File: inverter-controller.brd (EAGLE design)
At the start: 96 x 87 mm, 164 parts, among them IC1 STM32F334C8T6, IC10 ISO3082, IC2 SY7152ABC, IC3 LMV358MMX, IC4 LMV358MMX, IC5 SY7152ABC, J1 621006245821, J2 61300211121, J3 CONNECTOR-SMD-2PIN, J4 CONNECTOR-SMD-2PIN, J5 CONNECTOR-SMD-2PIN, X3 0289-9068**15EDGVC-3.81-03P-14, X6 1365-16, Y1 NX2016SA-32M

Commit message: Opamp devreleri düzenlendi.
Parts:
- moved DC7 804.7 mm to (37.5, 50.6)
- moved C66 789.4 mm to (40.3, 60.0)
- moved R65 780.3 mm to (40.3, 62.2), turned to 180 degrees
- moved TP8 780.1 mm to (36.1, 35.4), turned to 270 degrees
- moved C61 775.3 mm to (39.0, 35.4)
- moved TP11 773.5 mm to (35.0, 45.5)
- moved C60 767.9 mm to (39.0, 33.3), turned to 180 degrees
- moved C50 760.8 mm to (32.4, 33.1), turned to 180 degrees
- moved TP7 758.8 mm to (36.0, 33.3), turned to 270 degrees
- moved R69 757.8 mm to (29.8, 36.1), turned to 90 degrees
- moved R48 755.7 mm to (43.7, 41.5), turned to 90 degrees
- moved C53 754.8 mm to (45.0, 52.9), turned to 90 degrees
- moved L1 754.1 mm to (34.2, 48.3)
- moved R66 749.6 mm to (30.8, 38.9)
- moved R41 747.0 mm to (34.1, 42.3)
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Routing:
- net IA: track 0.00 -> 29.0 mm
- net N$20: track 0.00 -> 20.9 mm
- net I_IN: track 3.49 -> 23.0 mm
- net VB: track 0.00 -> 18.9 mm
- net VA: track 0.00 -> 15.5 mm
- net VOUT: track 0.00 -> 13.7 mm
- net IB: track 3.90 -> 12.4 mm
- net VIN_2: track 0.00 -> 8.41 mm
- net VIN_1: track 3.57 -> 11.4 mm
- net GND: track 0.00 -> 7.61 mm
- net N$15: track 0.00 -> 5.77 mm
- net N$21: track 0.00 -> 5.54 mm
- net N$19: track 0.00 -> 5.40 mm
- net IB_SENS: track 0.00 -> 5.05 mm, vias 0 -> 1
- net VB_SENS: track 0.00 -> 5.03 mm, vias 0 -> 1
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
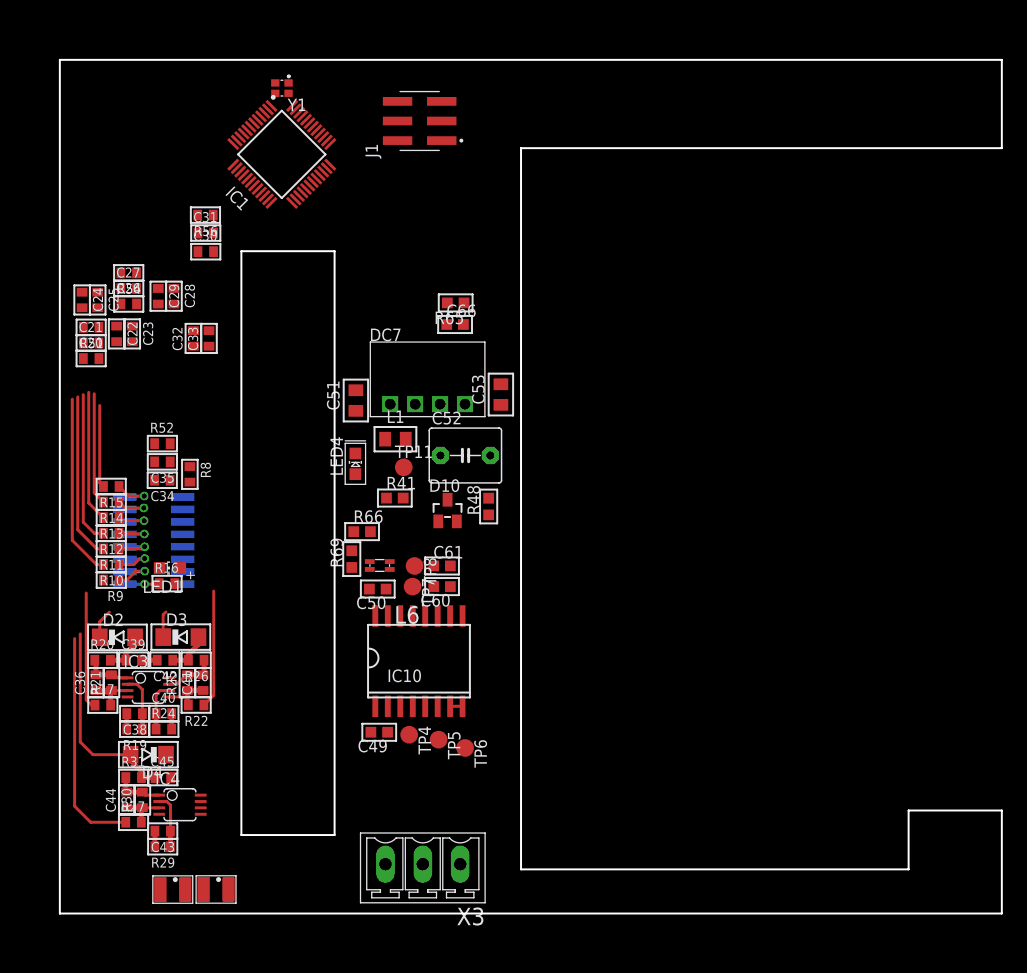
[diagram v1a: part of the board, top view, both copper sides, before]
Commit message: Dxf dosyasi cizimin uzerine eklendi, kart boyutlarinda duzenleme yapildi.
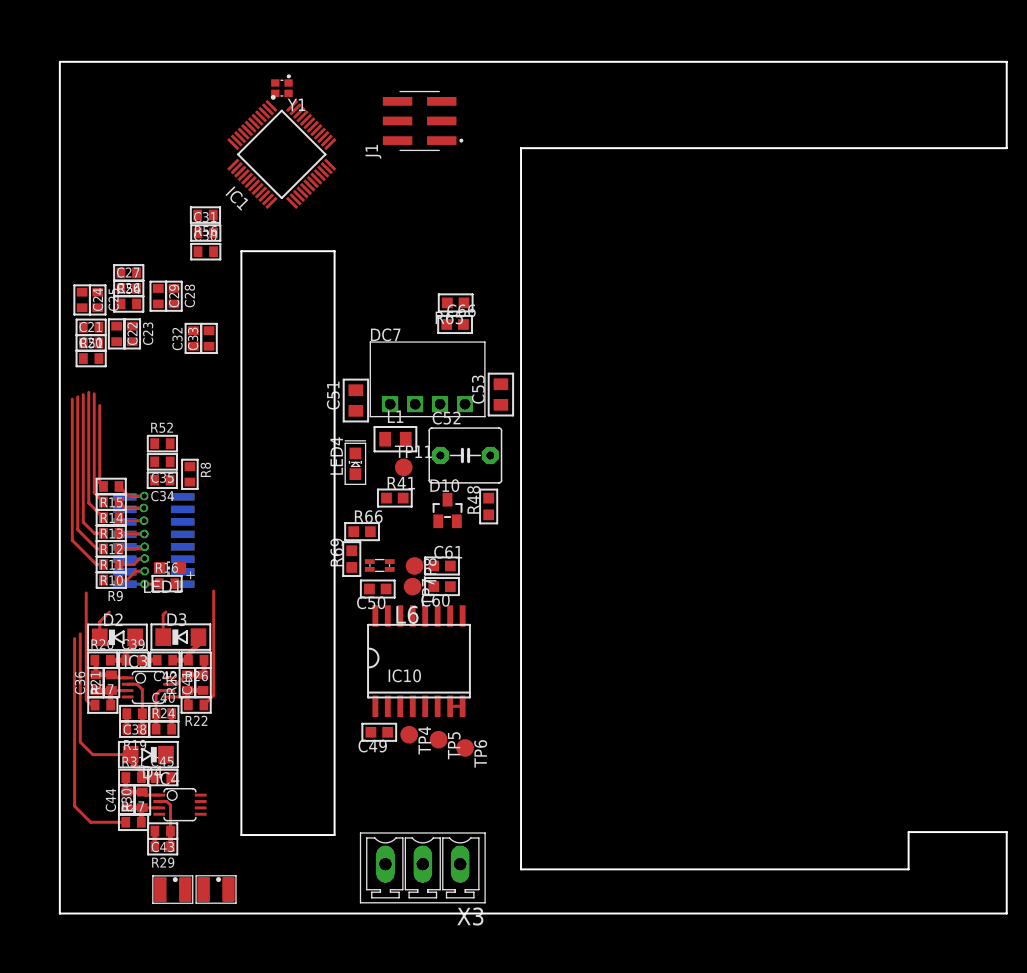
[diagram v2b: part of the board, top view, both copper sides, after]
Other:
- board size 96 x 87 mm -> 96.5 x 86.8 mm

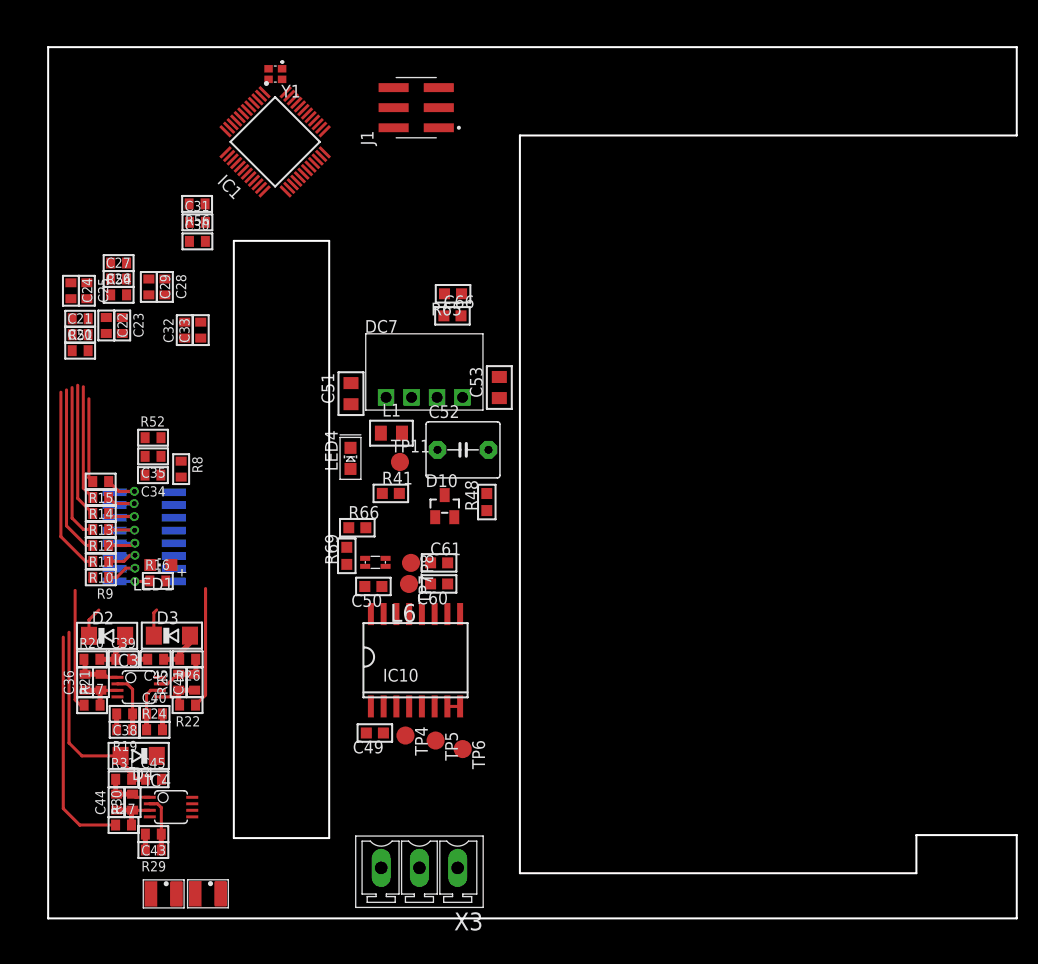
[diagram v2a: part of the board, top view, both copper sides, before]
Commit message: Kart baglanti pad'leri eklendi.
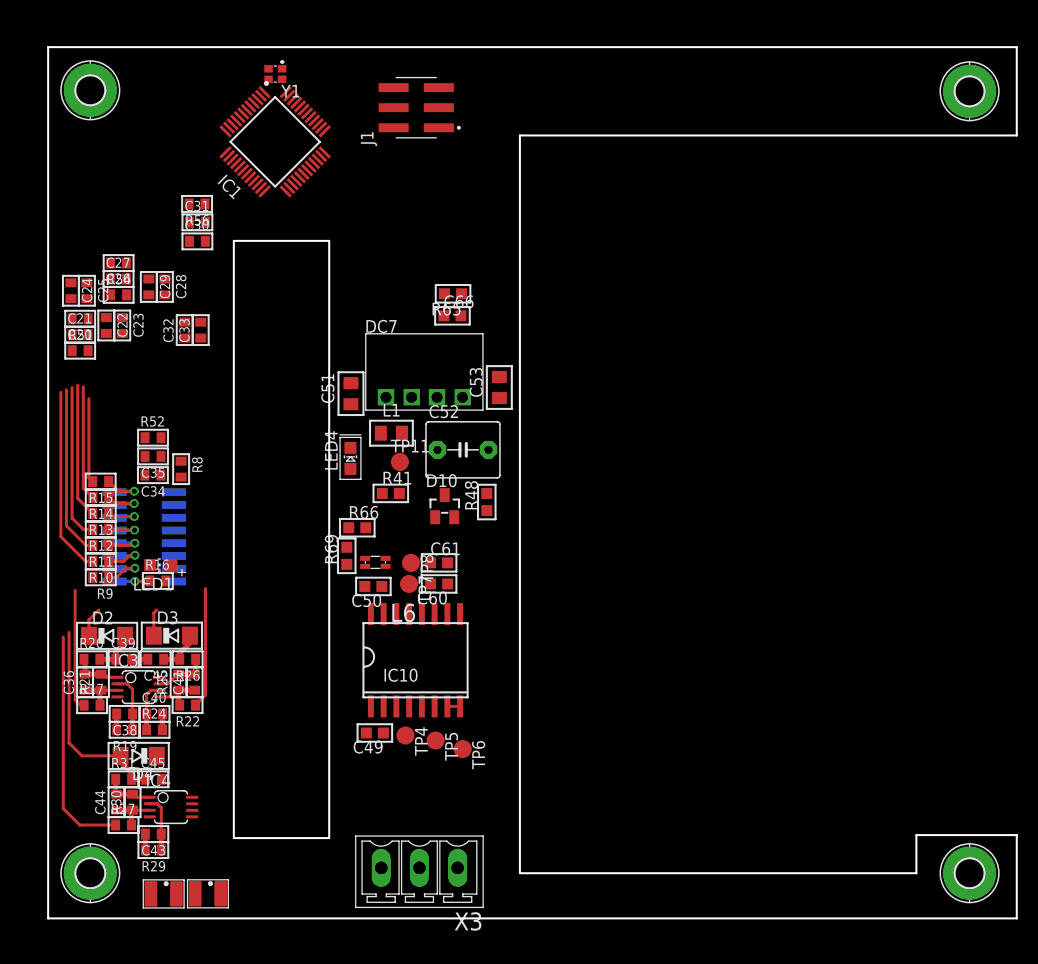
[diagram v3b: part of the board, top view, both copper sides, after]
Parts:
- added H1, H2, H3, H4: MOUNT-PAD-ROUND2.8, holes:2,8-PAD
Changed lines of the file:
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@@
 </element>
 <element name="J5" library="Andromeda" library_urn="urn:adsk.eagle:library:27258842" package="CONNECTOR-SMD-2PIN" value="CONNECTOR-SMD-2PIN" x="-159.89" y="-58.22" smashed="yes"/>
+<element name="H1" library="holes" library_urn="urn:adsk.eagle:library:237" package="2,8-PAD" package3d_urn="urn:adsk.eagle:package:14281/1" value="MOUNT-PAD-ROUND2.8" x="4.2" y="4.5" smashed="yes">
+<attribute name="POPULARITY" value="6" x="4.2" y="4.5" size="1.778" layer="27" font="vector" display="off"/>
+</element>
+<element name="H2" library="holes" library_urn="urn:adsk.eagle:library:237" package="2,8-PAD" package3d_urn="urn:adsk.eagle:package:14281/1" value="MOUNT-PAD-ROUND2.8" x="4.2" y="82.5" smashed="yes">
+<attribute name="POPULARITY" value="6" x="4.2" y="82.5" size="1.778" layer="27" font="vector" display="off"/>
+</element>
+<element name="H3" library="holes" library_urn="urn:adsk.eagle:library:237" package="2,8-PAD" package3d_urn="urn:adsk.eagle:package:14281/1" value="MOUNT-PAD-ROUND2.8" x="91.8" y="4.5" smashed="yes">
+<attribute name="POPULARITY" value="6" x="91.8" y="4.5" size="1.778" layer="27" font="vector" display="off"/>
+</element>
+<element name="H4" library="holes" library_urn="urn:adsk.eagle:library:237" package="2,8-PAD" package3d_urn="urn:adsk.eagle:package:14281/1" value="MOUNT-PAD-ROUND2.8" x="91.8" y="82.4" smashed="yes">
+<attribute name="POPULARITY" value="6" x="91.8" y="82.4" size="1.778" layer="27" font="vector" display="off"/>
+</element>
 </elements>
 <signals>

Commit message: RC Filtreleri ve Decoupling Cap. yerleştirildi.
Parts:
- moved C7 350.1 mm to (20.2, 71.1), turned to 135 degrees
- moved C9 348.4 mm to (28.9, 74.8), turned to 45 degrees
- moved C6 344.1 mm to (19.1, 70.0), turned to 135 degrees
- moved C8 343.5 mm to (30.0, 73.7), turned to 45 degrees
- moved C5 339.4 mm to (16.8, 80.9), turned to 225 degrees
- moved C3 336.4 mm to (14.0, 88.9), turned to 180 degrees
- moved C4 335.5 mm to (15.7, 82.0), turned to 225 degrees
- moved C2 333.3 mm to (13.6, 90.6)
- moved C1 330.5 mm to (12.9, 92.9), turned to 270 degrees
- moved R1 322.0 mm to (39.9, 73.0)
- moved C10 318.9 mm to (25.3, 83.2), turned to 135 degrees
- moved C11 316.1 mm to (26.4, 84.3), turned to 135 degrees
- moved R3 313.4 mm to (30.3, 83.9), turned to 270 degrees
- moved R2 312.6 mm to (37.4, 83.4), turned to 270 degrees
- moved TP1 126.3 mm to (11.8, 73.9)
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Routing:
- net VIN_2: track 8.41 -> 0.00 mm

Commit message: Fan Controller-2 yerleşimi yapıldı
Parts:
- moved C48 532.6 mm to (6.64, 52.5)
- moved C47 529.6 mm to (6.65, 54.4)
- moved R40 521.3 mm to (6.64, 50.7), turned to 180 degrees
- moved R39 518.0 mm to (9.20, 51.5), turned to 90 degrees
- moved R38 513.7 mm to (11.0, 51.5), turned to 90 degrees
- moved R35 509.5 mm to (12.9, 51.5), turned to 90 degrees
- moved R34 499.4 mm to (16.7, 51.6), turned to 90 degrees
- moved R33 494.1 mm to (15.1, 51.6), turned to 90 degrees
- moved C19 393.8 mm to (12.2, 4.83)
- moved R7 387.4 mm to (9.62, 2.56), turned to 90 degrees
- moved R28 361.5 mm to (13.0, 7.52), turned to 270 degrees
- moved C54 231.0 mm to (40.3, 60.8), turned to 180 degrees
- moved C56 229.3 mm to (40.3, 64.5), turned to 180 degrees
- moved R43 228.6 mm to (38.2, 54.6), turned to 90 degrees
- moved IC5 224.3 mm to (39.2, 58.1)
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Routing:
- net +3V3: track 4.12 -> 77.0 mm
- net RS485_ISO_GND: track 0.00 -> 58.4 mm, vias 0 -> 3
- net GND: track 7.61 -> 63.1 mm
- net N$34: track 0.00 -> 50.6 mm
- net IB: track 12.4 -> 62.5 mm, vias 0 -> 3
- net N$10: track 0.00 -> 46.2 mm
- net VB: track 18.9 -> 60.4 mm
- net VA: track 15.5 -> 57.0 mm, vias 0 -> 2
- net HRTIM1_FLT1: track 5.65 -> 46.2 mm, vias 0 -> 1
- net RS485_ISO_5V: track 0.00 -> 36.3 mm
- net G14_PWM: track 0.00 -> 33.9 mm
- net VOUT: track 13.7 -> 46.4 mm
- net G13_PWM: track 0.00 -> 31.7 mm
- net G12_PWM: track 0.00 -> 27.9 mm
- net IA: track 29.0 -> 55.7 mm, vias 0 -> 2
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
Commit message: Fan Controller-2 yerleşimi yapıldı
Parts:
- moved LED2 510.9 mm to (15.2, 58.3)
- moved R32 506.8 mm to (15.2, 54.9), turned to 90 degrees
- moved C16 486.3 mm to (12.7, 54.1), turned to 180 degrees
- moved C15 483.3 mm to (12.7, 56.0), turned to 180 degrees
- moved C18 480.3 mm to (12.7, 57.8), turned to 180 degrees
- moved C17 477.3 mm to (12.7, 59.7), turned to 180 degrees
- moved R6 466.8 mm to (8.90, 54.8), turned to 270 degrees
- moved R5 461.6 mm to (7.41, 54.8), turned to 90 degrees
- moved C14 460.7 mm to (10.3, 61.6)
- moved R4 459.1 mm to (10.4, 54.8), turned to 90 degrees
- moved C13 457.7 mm to (10.3, 63.4)
- moved C12 454.8 mm to (10.3, 65.3)
- moved R23 341.8 mm to (13.6, 18.6), turned to 180 degrees
- moved R18 303.5 mm to (4.13, 18.6)
- moved R55 229.8 mm to (39.1, 50.4), turned to 90 degrees
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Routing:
- net +3V3: track 77.0 -> 208.0 mm, vias 1 -> 5
- net GND: track 63.1 -> 126.7 mm, vias 0 -> 8
- net NTC1: track 5.10 -> 67.3 mm, vias 0 -> 5
- net N$28: track 0.00 -> 55.1 mm
- net N$27: track 0.00 -> 49.8 mm
- net I_IN: track 31.5 -> 66.7 mm, vias 0 -> 1
- net RS485_DIR: track 3.68 -> 27.7 mm, vias 0 -> 1
- net RS485_RX: track 3.66 -> 27.5 mm, vias 0 -> 1
- net +12V/2: track 0.00 -> 22.9 mm
- net RS485_TX: track 3.00 -> 25.7 mm, vias 0 -> 1
- net +12V/1: track 1.60 -> 13.4 mm
- net N$10: track 46.2 -> 55.2 mm
- net IA: track 55.7 -> 62.1 mm, vias 2 -> 4
- net N$8: track 0.00 -> 4.96 mm
- net N$25: track 0.00 -> 4.94 mm
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
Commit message: Programlama soketi degistirildi.
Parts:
- removed J1: 621006245821, Headers:621006245821
- added JP1: (no value), adafruit:1X06
- moved C46 402.8 mm to (12.5, 23.0), flipped to the bottom, turned to 270 degrees
- moved C37 331.0 mm to (13.8, 15.1), turned to 90 degrees
- moved R37 309.0 mm to (26.5, 91.1)
- moved R36 308.0 mm to (31.4, 90.5)
- moved LED12 205.8 mm to (31.5, 92.4), turned to 90 degrees
- moved LED8 197.6 mm to (26.5, 92.8), turned to 90 degrees
- moved C3 8.97 mm to (15.9, 84.4), turned to 135 degrees
- moved TP3 2.87 mm to (9.44, 72.0)
- moved TP2 1.28 mm to (11.0, 72.9)
- moved TP1 1.02 mm to (11.3, 74.8), turned to 270 degrees
- moved C8 0.75 mm to (29.5, 73.2)
- moved C9 0.74 mm to (28.3, 74.3)
- moved R3 0.52 mm to (30.3, 84.4)
- moved TP11 0.52 mm to (45.0, 55.5)
- moved C10 0.36 mm to (25.1, 83.5)
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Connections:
- removed net N$11: J1.1, R1.2
- new net N$30: JP1.1, R1.2
- net GND: now also JP1.3; no longer J1.3
- net NRST: now also JP1.5; no longer J1.5
- net SWCLK: now also JP1.2; no longer J1.2
- net SWDIO: now also JP1.4; no longer J1.4
- net SWO: now also JP1.6; no longer J1.6
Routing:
- net I_FAN: track 3.72 -> 32.0 mm, vias 0 -> 2
- net RS485_RX: track 27.5 -> 53.0 mm, vias 1 -> 2
- net FAN1_EN: track 2.20 -> 27.3 mm
- net +3V3: track 208.0 -> 233.0 mm, vias 5 -> 7
- net RS485_LED: track 2.74 -> 27.4 mm
- net RS485_TX: track 25.7 -> 48.9 mm, vias 1 -> 6
- net RS485_DIR: track 27.7 -> 49.9 mm, vias 1 -> 2
- net NTC1: track 67.3 -> 84.0 mm, vias 5 -> 6
- net G14_PWM: track 33.9 -> 48.7 mm
- net GND: track 126.7 -> 139.7 mm, vias 8 -> 13
- net N$5: track 0.00 -> 10.7 mm
- net N$6: track 0.00 -> 8.67 mm
- net N$4: track 0.00 -> 8.51 mm
- net N$3: track 0.00 -> 7.27 mm
- net NRST: track 0.00 -> 4.88 mm
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- added copper zone on layer 16, net GND
